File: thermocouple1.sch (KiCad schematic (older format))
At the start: 2 parts

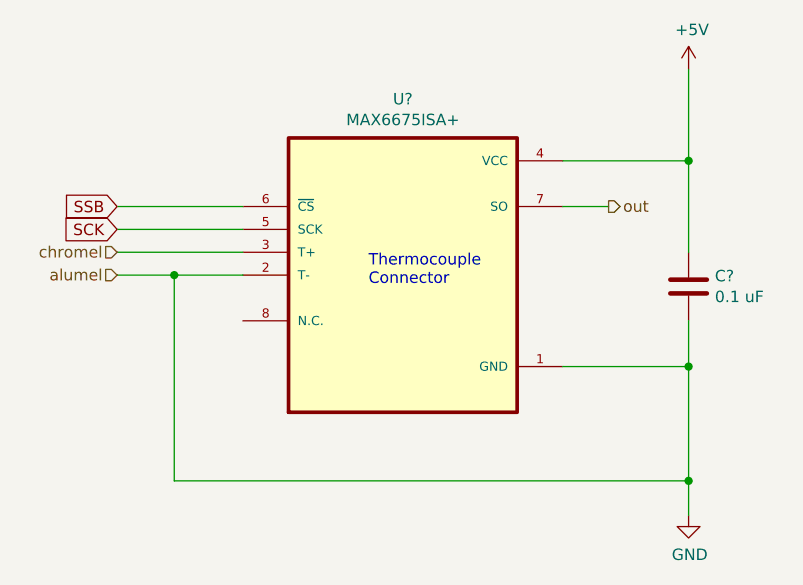
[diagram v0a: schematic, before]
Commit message: updated SCK
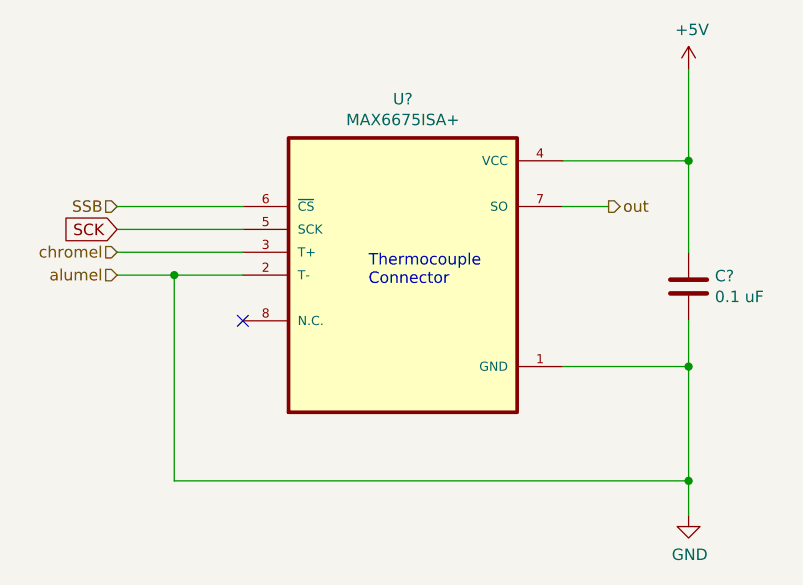
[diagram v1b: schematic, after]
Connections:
- no-connect marks 0 -> 1
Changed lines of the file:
@@
 Comment4 ""
 $EndDescr
-Text GLabel 4250 3650 0    50   Input ~ 0
-SCK
-Text GLabel 4250 3550 0    50   Input ~ 0
-SSB
 Connection ~ 6750 4250
 $Comp
@@
 Text HLabel 4250 3850 0    50   Input ~ 0
 alumel
+Text HLabel 4250 3550 0    50   Input ~ 0
+SSB
+NoConn ~ 4800 4050
+Text GLabel 4250 3650 0    50   Input ~ 0
+SCK
 $EndSCHEMATC
